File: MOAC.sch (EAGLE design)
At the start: 56 parts, among them IC1 ATMEGA32U4NT-TQFP, J1 3.5mm, J2 3.5mm, J3 3.5mm, J4 3.5mm, J5 3.5mm, J6 3.5mm, J7 3.5mm, J8 3.5mm, J9 USB-C

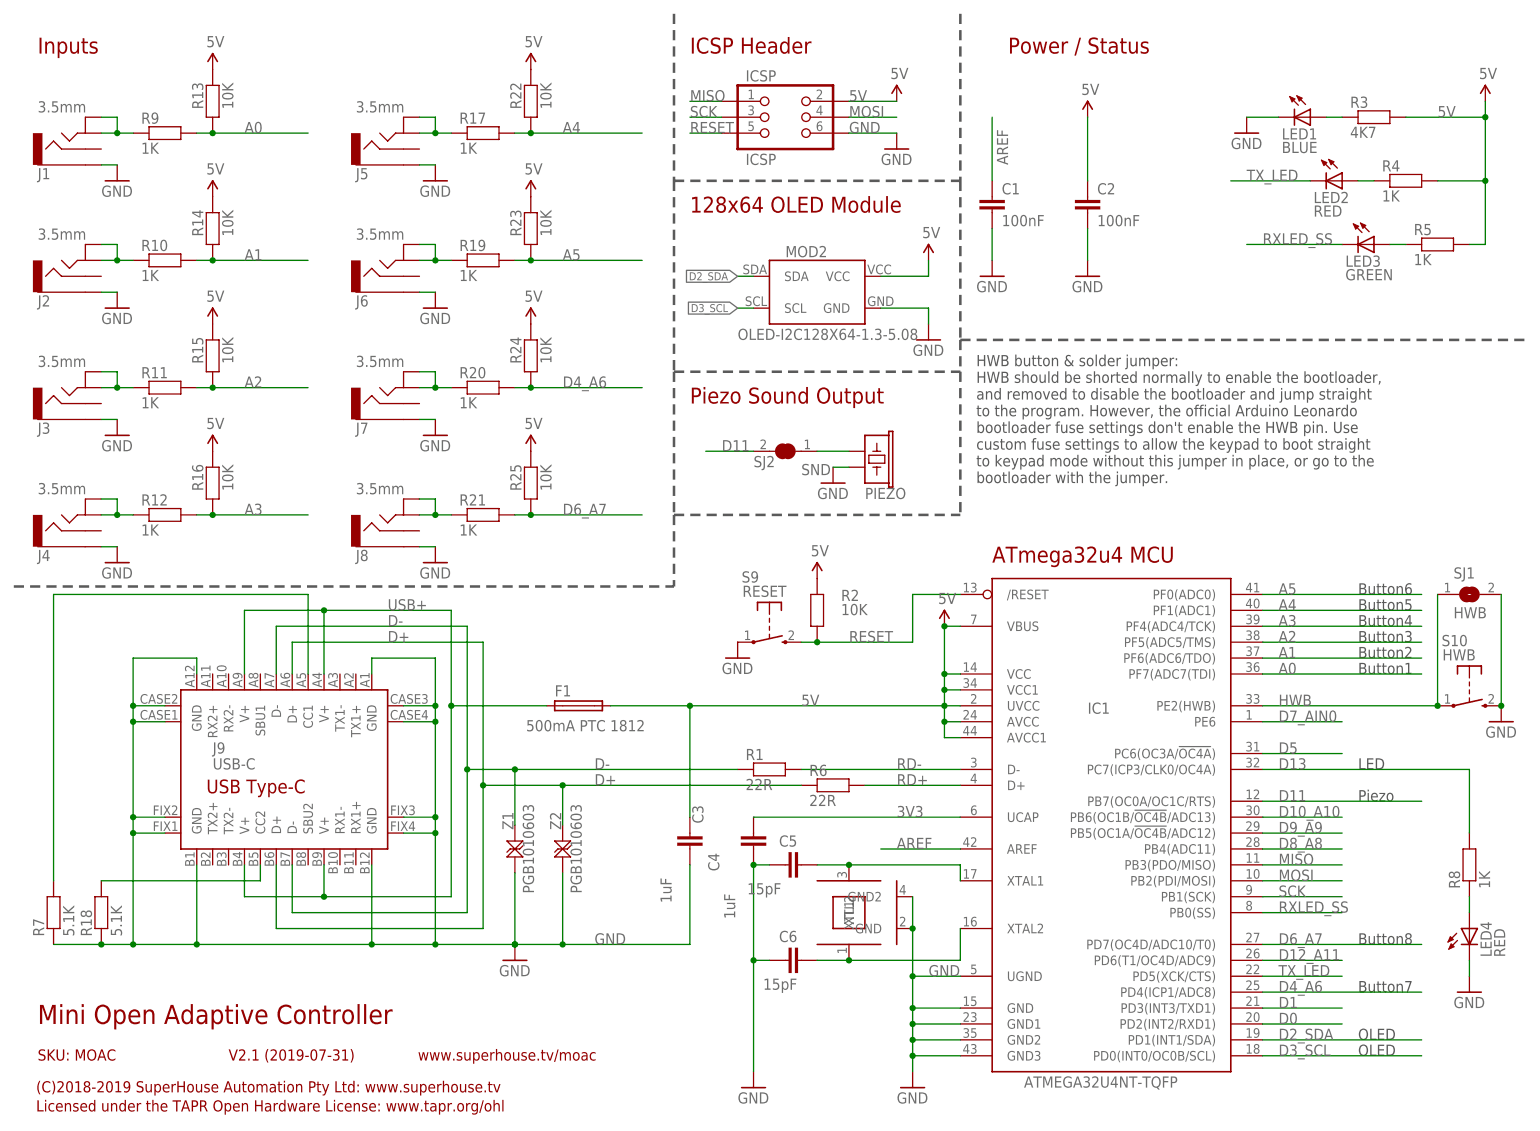
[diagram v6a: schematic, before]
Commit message: Added piezo switch; replaced USB-C socket for v2.1 release
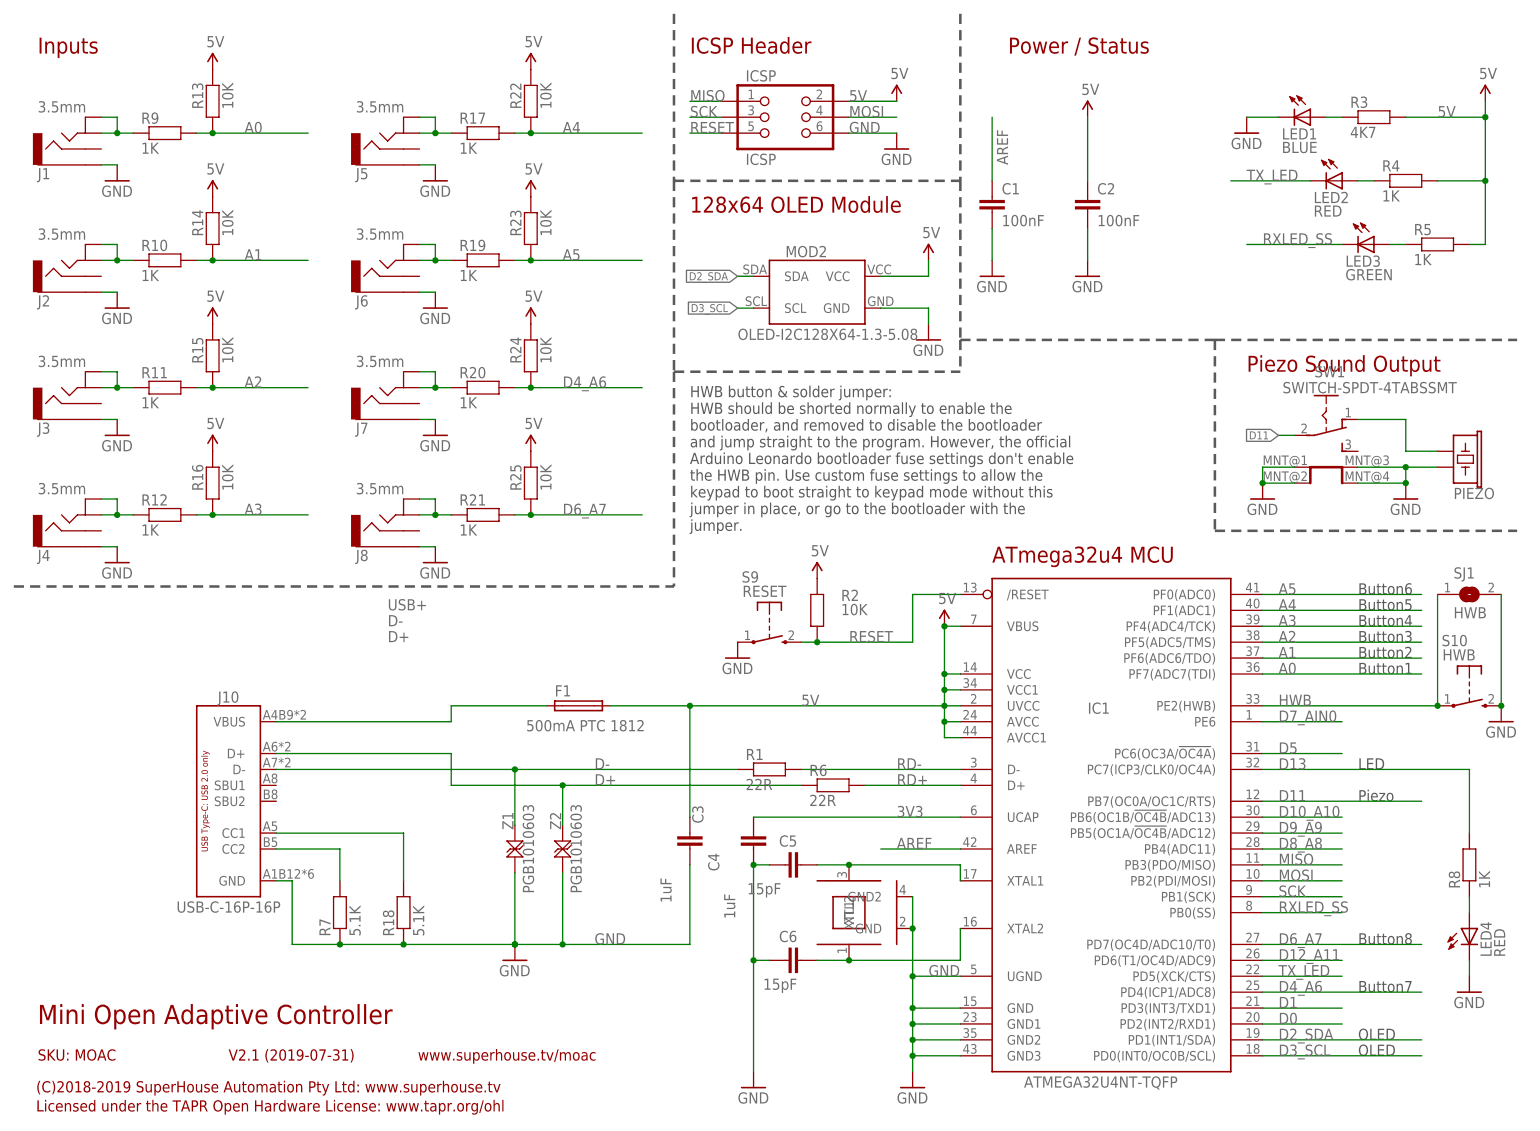
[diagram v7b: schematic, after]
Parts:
- removed J9: USB-C, SuperHouse-Connectors:USB-C
- removed SJ2: SND, SuperHouse-Jumpers:SJC-NORMAL
- added J10: USB-C-16P-16P, SuperHouse-Connectors:USB-C-16P-16P
- added SW1: SWITCH-SPDT-4TABSSMT, SuperHouse-Switches:SWITCH-SPDT-4TABSSMT
- C3: device SuperHouse-DiscreteSemi:CAP0603 -> SuperHouse-DiscreteSemi:CAP0805
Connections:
- removed net N$67: J9.CC1, R7.2
- new net N$17: J10.CC1, R18.2
- net D+: now also J10.D+; no longer J9.D+@A6, J9.D+@B6
- net D-: now also J10.D-; no longer J9.D-@A7, J9.D-@B7
- net D11: now also SW1.COM; no longer SJ2.2
- net GND: now also J10.GND, SW1.MNT@1, SW1.MNT@2, SW1.MNT@3, SW1.MNT@4; no longer J9.GND@A1, J9.GND@A12, J9.GND@B1, J9.GND@B12, J9.GND@CASE1, J9.GND@CASE2, J9.GND@CASE3, J9.GND@CASE4, J9.GND@FIX1, J9.GND@FIX2, J9.GND@FIX3, J9.GND@FIX4
- net N$1: now also J10.CC2, R7.2; no longer J9.CC2, R18.2
- net N$16: now also SW1.A; no longer SJ2.1
- net USB+: now also J10.VBUS; no longer J9.V+@A4, J9.V+@A9, J9.V+@B4, J9.V+@B9
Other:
- moved on the sheet: PIEZO, R18, R7

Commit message: Final tweaks and DRC for v2.1 release
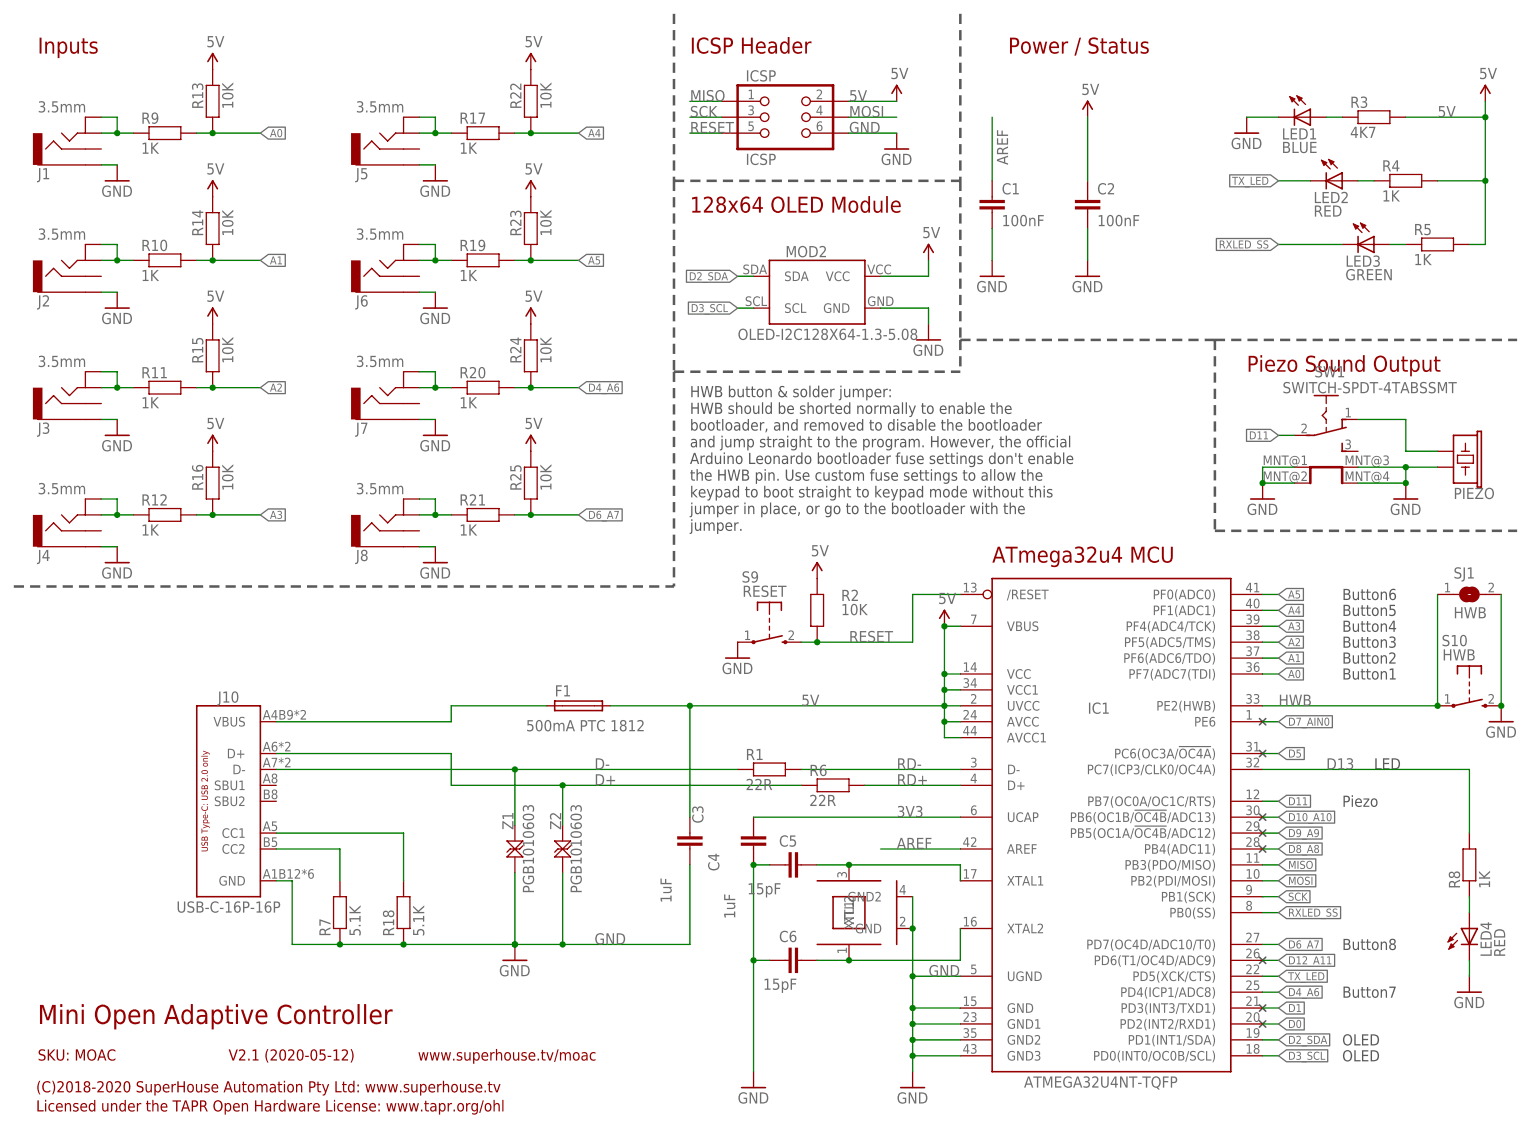
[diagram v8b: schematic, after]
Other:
- note added: "(C)2018-2020 SuperHouse Automation Pty Ltd: www.superhouse.tv"
- note added: "V2.1 (2020-05-12)"
- note removed: "(C)2018-2019 SuperHouse Automation Pty Ltd: www.superhouse.tv"
- note removed: "V2.1 (2019-07-31)"
